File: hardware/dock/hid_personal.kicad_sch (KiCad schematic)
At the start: 15 parts, among them J3 Conn_01x05_Pin, J4 L-KLS1-5416-L1-01-R, U5 TPD4E1U06DBVR

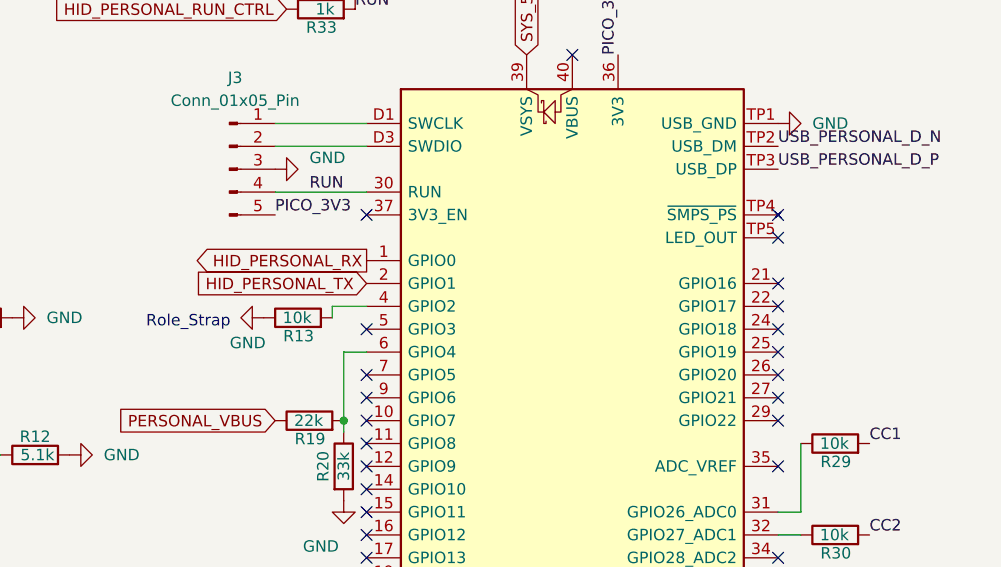
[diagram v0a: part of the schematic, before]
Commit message: Re-pin host/endpoint GPIOs by PCB position; update placement guide
- Host A1: HID-A UART0 -> GP12/13, HID-B UART1 -> GP20/21, BLE PIO ->
  GP16/17, KEYBOARD_VBUS_EN/FAULT -> GP26/27, MUX_STATUS -> GP28,
  POGO_5V_FAULT -> GP18, HID_PERSONAL_RUN_CTRL -> GP2,
  HID_WORK_RUN_CTRL -> GP19 (BLE_RST_CTRL stays GP22)
- HID-A UART0 -> GP16/17, HID-B UART0 -> GP12/13 (pins facing the host)
- Ratsnest crossings on current placement 132 -> 95
- DESIGN.md pin tables updated; PCB_PLACEMENT.md: pull-up/pull-down
  placement, Pico GPIO map, 100x100 outline, routing techniques
- Stop tracking KiCad _restore_backup_* folders (kept on disk, ignored)

Co-Authored-By: Claude Opus 5.5 <noreply@anthropic.com>
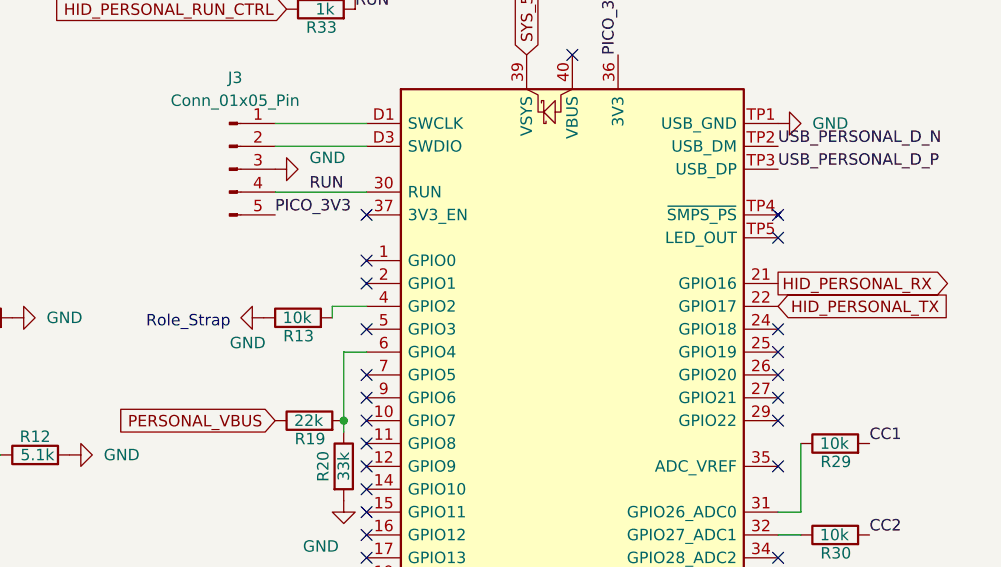
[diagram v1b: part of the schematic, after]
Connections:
- net HID_PERSONAL_RX: now also A2.21 (GPIO16); no longer A2.1 (GPIO0)
- net HID_PERSONAL_TX: now also A2.22 (GPIO17); no longer A2.2 (GPIO1)
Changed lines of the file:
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@@
-	)
-	(no_connect
-		(at 152.4 88.9)
 	)
 	(no_connect
@@
 	(no_connect
 		(at 40.64 87.63)
-	)
-	(no_connect
-		(at 152.4 86.36)
 	)
 	(no_connect
@@
 				)
 				(justify left)
-			)
-		)
-	)
-	(global_label "HID_PERSONAL_TX"
-		(shape input)
-		(at 106.68 86.36 180)
-		(fields_autoplaced yes)
-		(effects
-			(font
-				(size 1.27 1.27)
-			)
-			(justify right)
-		)
-		(property "Intersheetrefs" "${INTERSHEET_REFS}"
-			(at 86.3986 86.36 0)
-			(hide yes)
-			(show_name no)
-			(do_not_autoplace no)
-			(effects
-				(font
-					(size 1.27 1.27)
-				)
-				(justify right)
-			)
-		)
-	)
-	(global_label "HID_PERSONAL_RX"
-		(shape output)
-		(at 106.68 83.82 180)
-		(fields_autoplaced yes)
-		(effects
-			(font
-				(size 1.27 1.27)
-			)
-			(justify right)
-		)
-		(property "Intersheetrefs" "${INTERSHEET_REFS}"
-			(at 86.701 83.82 0)
-			(hide yes)
-			(show_name no)
-			(do_not_autoplace no)
-			(effects
-				(font
-					(size 1.27 1.27)
-				)
-				(justify right)
 			)
 		)
@@
 		)
 	)
+	(global_label "HID_PERSONAL_RX"
+		(shape output)
+		(at 152.4 86.36 0)
+		(fields_autoplaced yes)
+		(effects
+			(font
+				(size 1.27 1.27)
+			)
+			(justify left)
+		)
+		(property "Intersheetrefs" "${INTERSHEET_REFS}"
+			(at 152.4 86.36 0)
+			(hide yes)
+			(show_name no)
+			(do_not_autoplace no)
+			(effects
+				(font
+					(size 1.27 1.27)
+				)
+				(justify left)
+			)
+		)
+	)
+	(global_label "HID_PERSONAL_TX"
+		(shape input)
+		(at 152.4 88.9 0)
+		(fields_autoplaced yes)
+		(effects
+			(font
+				(size 1.27 1.27)
+			)
+			(justify left)
+		)
+		(property "Intersheetrefs" "${INTERSHEET_REFS}"
+			(at 152.4 88.9 0)
+			(hide yes)
+			(show_name no)
+			(do_not_autoplace no)
+			(effects
+				(font
+					(size 1.27 1.27)
+				)
+				(justify left)
+			)
+		)
+	)
+	(no_connect
+		(at 106.68 86.36)
+	)
+	(no_connect
+		(at 106.68 83.82)
+	)
 )

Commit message: Host becomes Pico 2 W (on-board BLE); remove XIAO nRF52840
- A1 -> Raspberry Pi Pico 2 W, new footprint RaspberryPi_Pico2W_Socket_Pogo
  (TP1-3 probes unchanged, SWD via 1x3 socket under the debug holes,
  TP4-6 at Pico 2 W positions, 14x9 mm antenna keep-out)
- Remove U7 (XIAO), J8 and R35; BLE UART and BLE_RST_CTRL gone
- Pogo TX/RX/DET now go to the host: GP16 (PIO TX), GP17 (PIO RX),
  GP22 (DET); R18 pulls DET up to HOST_3V3
- HID-A: CC1/CC2 on U5 and R29/R30 swapped for routing (user change)
- DESIGN.md/README/PCB_PLACEMENT.md updated; board includes in-progress
  routing and B.Cu GND zone (not yet updated from schematic)

Co-Authored-By: Claude Opus 5.5 <noreply@anthropic.com>
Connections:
- net CC1: now also R30.2, U5.3 (D2+); no longer R29.2, U5.4 (D2-)
- net CC2: now also R29.2, U5.4 (D2-); no longer R30.2, U5.3 (D2+)
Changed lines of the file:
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@@
+	)
+	(no_connect
+		(at 106.68 83.82)
 	)
 	(no_connect
@@
 	(no_connect
 		(at 152.4 106.68)
+	)
+	(no_connect
+		(at 106.68 86.36)
 	)
 	(no_connect
@@
 			(width 0)
 			(type default)
-		)
-	)
-	(label "CC1"
-		(at 162.56 104.14 0)
-		(effects
-			(font
-				(size 1.27 1.27)
-			)
-			(justify left bottom)
 		)
 	)
@@
 		)
 	)
+	(label "CC1"
+		(at 162.56 114.3 0)
+		(effects
+			(font
+				(size 1.27 1.27)
+			)
+			(justify left bottom)
+		)
+	)
 	(label "USB_PERSONAL_D_N"
 		(at 40.64 97.79 0)
@@
 		)
 	)
-	(label "CC1"
+	(label "CC2"
 		(at 45.72 69.85 180)
 		(effects
@@
 			)
 			(justify right bottom)
+		)
+	)
+	(label "CC2"
+		(at 162.56 104.14 0)
+		(effects
+			(font
+				(size 1.27 1.27)
+			)
+			(justify left bottom)
 		)
 	)
@@
 		)
 	)
+	(label "CC1"
+		(at 45.72 67.31 180)
+		(effects
+			(font
+				(size 1.27 1.27)
+			)
+			(justify right bottom)
+		)
+	)
 	(label "USB_PERSONAL_D_P"
 		(at 152.4 73.66 0)
@@
 		)
 	)
-	(label "CC2"
-		(at 162.56 114.3 0)
-		(effects
-			(font
-				(size 1.27 1.27)
-			)
-			(justify left bottom)
-		)
-	)
 	(label "USB_PERSONAL_D_N"
 		(at 45.72 64.77 180)
@@
 			)
 			(justify left bottom)
-		)
-	)
-	(label "CC2"
-		(at 45.72 67.31 180)
-		(effects
-			(font
-				(size 1.27 1.27)
-			)
-			(justify right bottom)
 		)
 	)
@@
 		)
 	)
+	(global_label "HID_PERSONAL_RX"
+		(shape output)
+		(at 152.4 86.36 0)
+		(fields_autoplaced yes)
+		(effects
+			(font
+				(size 1.27 1.27)
+			)
+			(justify left)
+		)
+		(property "Intersheetrefs" "${INTERSHEET_REFS}"
+			(at 152.4 86.36 0)
+			(hide yes)
+			(show_name no)
+			(do_not_autoplace no)
+			(effects
+				(font
+					(size 1.27 1.27)
+				)
+				(justify left)
+			)
+		)
+	)
 	(global_label "HID_PERSONAL_RUN_CTRL"
 		(shape input)
@@
 		(property "Intersheetrefs" "${INTERSHEET_REFS}"
 			(at 65.5176 85.09 0)
+			(hide yes)
+			(show_name no)
+			(do_not_autoplace no)
+			(effects
+				(font
+					(size 1.27 1.27)
+				)
+				(justify left)
+			)
+		)
+	)
+	(global_label "HID_PERSONAL_TX"
+		(shape input)
+		(at 152.4 88.9 0)
+		(fields_autoplaced yes)
+		(effects
+			(font
+				(size 1.27 1.27)
+			)
+			(justify left)
+		)
+		(property "Intersheetrefs" "${INTERSHEET_REFS}"
+			(at 152.4 88.9 0)
 			(hide yes)
 			(show_name no)
@@
 		)
 	)
-	(global_label "HID_PERSONAL_RX"
-		(shape output)
-		(at 152.4 86.36 0)
-		(fields_autoplaced yes)
-		(effects
-			(font
-				(size 1.27 1.27)
-			)
-			(justify left)
-		)
-		(property "Intersheetrefs" "${INTERSHEET_REFS}"
-			(at 152.4 86.36 0)
-			(hide yes)
-			(show_name no)
-			(do_not_autoplace no)
-			(effects
-				(font
-					(size 1.27 1.27)
-				)
-				(justify left)
-			)
-		)
-	)
-	(global_label "HID_PERSONAL_TX"
-		(shape input)
-		(at 152.4 88.9 0)
-		(fields_autoplaced yes)
-		(effects
-			(font
-				(size 1.27 1.27)
-			)
-			(justify left)
-		)
-		(property "Intersheetrefs" "${INTERSHEET_REFS}"
-			(at 152.4 88.9 0)
-			(hide yes)
-			(show_name no)
-			(do_not_autoplace no)
-			(effects
-				(font
-					(size 1.27 1.27)
-				)
-				(justify left)
-			)
-		)
-	)
-	(no_connect
-		(at 106.68 86.36)
-	)
-	(no_connect
-		(at 106.68 83.82)
-	)
 )
